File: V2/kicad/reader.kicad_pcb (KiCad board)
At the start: 2 copper layers, 42.5 x 62 mm, 93 parts, among them SW1 SW_Rezistance, SW2 SW_src, U1 STM32H523CET6, U2 MAX98357AETE+T, U3 MLD-TF PUSH-H18, U4 TCAN1057AVDRQ1, U5 ESD2CAN24-ES, U6 RJ-064-1, U7 MCP16301Hx-xCH, Y1 16MHz

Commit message: changed led red color resistor from 560 to 787
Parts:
- R15, R17: value 560 R -> 787 R
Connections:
- SW1 pad 2: (no net) -> unconnected-(SW1-Pad2)
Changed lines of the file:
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@@
 			)
 		)
-		(property "Value" "560 R"
+		(property "Value" "787 R"
 			(at 0 1.17 90)
 			(layer "F.Fab")
@@
 			)
 		)
-		(property "Datasheet" "https://jlc-prod-smt.oss-eu-central-1.aliyuncs.com/smtDataManualFile/8586178278474862592-C25126.pdf?response-content-disposition=attachment%3B%20filename%3DC25126.pdf%3B%20filename%2A%3DUTF-8%27%27C25126.pdf&x-oss-date=20260603T141942Z&x-oss-expires=1800&x-oss-security-token=CAISgAN1q6Ft5B2yfSjIr5rYAPaHqJFCjrvadU%2FFs1YWQtlZrr3lsTz2IHhMdHJsAOodtv0%2FmmhT6PkclqRLcbhpcmfjV%2BZHzLB8qeAa7RNB4J7b16cNrbH4M4H6aXeirtuwDsz9SNTCALjPD3nPii50x5bjaDymRCbLGJaViJlhHLN1Ow6jdmhpCctxLAlvo9NgFxm3D%2Fu2NQPwiWf9FVdhvhEG6Vly8qOi2MaRmFy8yFTx0b0SvJ%2BjYMrmPctoN9JnSdC5mfdzau3a1TJ84gRD0a5wkaVA1zbDs5bfISEIuUzebreLqY03dV4mOvdqIcMe8qigz88fk%2FfIioH6xyxKOexoSCnFTOiiupCcQLPyao9jLu6iayqViY7QaIOTqQohZmkAMwVOasAsI3Ngh4zF97Qt0cVNkXO9gWfLI8DtuMleWhqDHsNdntHD0eS19jklBdzSlusJRAJJUVBflCeKEaRNSAd3WGhEfM2%2BBt4QT30w5N2u00S8OSMIe8fo%2BKKWD5sagAFAjLTD0371Sd2gSdBnykA7MII9CzBs0TEnncOuMMFpZ7eWxtofkMZUw83MXKFT3yGfjS9fIlx%2Bre7vtwbXSVmucxBbZSJldeqhHVomhZC6FwsraIa5cFo%2FJ2rvy%2BYXQ1kdyLEoPt0fplni6hRiSJOL598AUZr9EPV4uuEaQBdebyAA&x-oss-signature-version=OSS4-HMAC-SHA256&x-oss-credential=STS.NYmKL3ENc9y1witWVCNVuAxNS%2F20260603%2Feu-central-1%2Foss%2Faliyun_v4_request&x-oss-signature=d1629a371fbf831c62f9f7f4032d37edb65e47d37709e76674d141769ad7b5bf"
+		(property "Datasheet" "https://www.lcsc.com/datasheet/C270582.pdf?spm=wm.sxq.inf.ggs___wm.fly.bg.0.xh&lcsc_vid=FVRbUlZVElUKAldUT1FbAVZWElcMUlFXR1FXBgVQElUxVlNeRlNeUVRXQFhZVTsOAxUeFF5JWBYZEEoKFBINSQcJGk4dAgUUFAk%3D"
 			(at 0 0 90)
 			(layer "F.Fab")
@@
 			)
 		)
-		(property "JLCPCB" "https://jlcpcb.com/partdetail/C25126"
+		(property "JLCPCB" "https://www.lcsc.com/product-detail/C270582.html"
 			(at 0 0 90)
 			(unlocked yes)
@@
 			)
 		)
-		(property "LCSC" "C25126"
+		(property "LCSC" "C270582"
 			(at 0 0 90)
 			(unlocked yes)
@@
 			(size 1.5 0.7)
 			(layers "F.Cu" "F.Mask" "F.Paste")
+			(net "unconnected-(SW1-Pad2)")
 			(pinfunction "2_2")
 			(pintype "passive+no_connect")
@@
 			)
 		)
-		(property "Value" "560 R"
+		(property "Value" "787 R"
 			(at 0 1.17 90)
 			(layer "F.Fab")
@@
 			)
 		)
-		(property "Datasheet" "https://jlc-prod-smt.oss-eu-central-1.aliyuncs.com/smtDataManualFile/8586178278474862592-C25126.pdf?response-content-disposition=attachment%3B%20filename%3DC25126.pdf%3B%20filename%2A%3DUTF-8%27%27C25126.pdf&x-oss-date=20260603T141942Z&x-oss-expires=1800&x-oss-security-token=CAISgAN1q6Ft5B2yfSjIr5rYAPaHqJFCjrvadU%2FFs1YWQtlZrr3lsTz2IHhMdHJsAOodtv0%2FmmhT6PkclqRLcbhpcmfjV%2BZHzLB8qeAa7RNB4J7b16cNrbH4M4H6aXeirtuwDsz9SNTCALjPD3nPii50x5bjaDymRCbLGJaViJlhHLN1Ow6jdmhpCctxLAlvo9NgFxm3D%2Fu2NQPwiWf9FVdhvhEG6Vly8qOi2MaRmFy8yFTx0b0SvJ%2BjYMrmPctoN9JnSdC5mfdzau3a1TJ84gRD0a5wkaVA1zbDs5bfISEIuUzebreLqY03dV4mOvdqIcMe8qigz88fk%2FfIioH6xyxKOexoSCnFTOiiupCcQLPyao9jLu6iayqViY7QaIOTqQohZmkAMwVOasAsI3Ngh4zF97Qt0cVNkXO9gWfLI8DtuMleWhqDHsNdntHD0eS19jklBdzSlusJRAJJUVBflCeKEaRNSAd3WGhEfM2%2BBt4QT30w5N2u00S8OSMIe8fo%2BKKWD5sagAFAjLTD0371Sd2gSdBnykA7MII9CzBs0TEnncOuMMFpZ7eWxtofkMZUw83MXKFT3yGfjS9fIlx%2Bre7vtwbXSVmucxBbZSJldeqhHVomhZC6FwsraIa5cFo%2FJ2rvy%2BYXQ1kdyLEoPt0fplni6hRiSJOL598AUZr9EPV4uuEaQBdebyAA&x-oss-signature-version=OSS4-HMAC-SHA256&x-oss-credential=STS.NYmKL3ENc9y1witWVCNVuAxNS%2F20260603%2Feu-central-1%2Foss%2Faliyun_v4_request&x-oss-signature=d1629a371fbf831c62f9f7f4032d37edb65e47d37709e76674d141769ad7b5bf"
+		(property "Datasheet" "https://www.lcsc.com/datasheet/C270582.pdf?spm=wm.sxq.inf.ggs___wm.fly.bg.0.xh&lcsc_vid=FVRbUlZVElUKAldUT1FbAVZWElcMUlFXR1FXBgVQElUxVlNeRlNeUVRXQFhZVTsOAxUeFF5JWBYZEEoKFBINSQcJGk4dAgUUFAk%3D"
 			(at 0 0 90)
 			(layer "F.Fab")
@@
 			)
 		)
-		(property "JLCPCB" "https://jlcpcb.com/partdetail/C25126"
+		(property "JLCPCB" "https://www.lcsc.com/product-detail/C270582.html"
 			(at 0 0 90)
 			(unlocked yes)
@@
 			)
 		)
-		(property "LCSC" "C25126"
+		(property "LCSC" "C270582"
 			(at 0 0 90)
 			(unlocked yes)
@@
 	)
 	(segment
+		(start 138.01 74.95)
+		(end 136.54 74.95)
+		(width 0.2)
+		(layer "F.Cu")
+		(net "/Net-(U1-VDDA)")
+	)
+	(segment
+		(start 138.65 75.59)
+		(end 138.01 74.95)
+		(width 0.2)
+		(layer "F.Cu")
+		(net "/Net-(U1-VDDA)")
+	)
+	(segment
+		(start 139.43595 73.28595)
+		(end 139.43595 75.00095)
+		(width 0.3)
+		(layer "F.Cu")
+		(net "/Net-(U1-VDDA)")
+	)
+	(segment
+		(start 139.7329 72.989)
+		(end 139.43595 73.28595)
+		(width 0.3)
+		(layer "F.Cu")
+		(net "/Net-(U1-VDDA)")
+	)
+	(segment
+		(start 140.8036 72.989)
+		(end 139.7329 72.989)
+		(width 0.3)
+		(layer "F.Cu")
+		(net "/Net-(U1-VDDA)")
+	)
+	(segment
+		(start 139.43595 75.00095)
+		(end 140.21 75.775)
+		(width 0.3)
+		(layer "F.Cu")
+		(net "/Net-(U1-VDDA)")
+	)
+	(segment
+		(start 138.65 75.59)
+		(end 138.8469 75.59)
+		(width 0.2)
+		(layer "F.Cu")
+		(net "/Net-(U1-VDDA)")
+	)
+	(segment
+		(start 138.8469 75.59)
+		(end 139.43595 75.00095)
+		(width 0.2)
+		(layer "F.Cu")
+		(net "/Net-(U1-VDDA)")
+	)
+	(segment
 		(start 164.51 35.63)
 		(end 164.51 35.314)
@@
 		(net "Net-(LED2-A2)")
 	)
-	(segment
-		(start 138.01 74.95)
-		(end 136.54 74.95)
-		(width 0.2)
-		(layer "F.Cu")
-		(net "/Net-(U1-VDDA)")
-	)
-	(segment
-		(start 138.65 75.59)
-		(end 138.01 74.95)
-		(width 0.2)
-		(layer "F.Cu")
-		(net "/Net-(U1-VDDA)")
-	)
-	(segment
-		(start 139.43595 73.28595)
-		(end 139.43595 75.00095)
-		(width 0.3)
-		(layer "F.Cu")
-		(net "/Net-(U1-VDDA)")
-	)
-	(segment
-		(start 139.7329 72.989)
-		(end 139.43595 73.28595)
-		(width 0.3)
-		(layer "F.Cu")
-		(net "/Net-(U1-VDDA)")
-	)
-	(segment
-		(start 140.8036 72.989)
-		(end 139.7329 72.989)
-		(width 0.3)
-		(layer "F.Cu")
-		(net "/Net-(U1-VDDA)")
-	)
-	(segment
-		(start 139.43595 75.00095)
-		(end 140.21 75.775)
-		(width 0.3)
-		(layer "F.Cu")
-		(net "/Net-(U1-VDDA)")
-	)
-	(segment
-		(start 138.65 75.59)
-		(end 138.8469 75.59)
-		(width 0.2)
-		(layer "F.Cu")
-		(net "/Net-(U1-VDDA)")
-	)
-	(segment
-		(start 138.8469 75.59)
-		(end 139.43595 75.00095)
-		(width 0.2)
-		(layer "F.Cu")
-		(net "/Net-(U1-VDDA)")
-	)
 	(zone

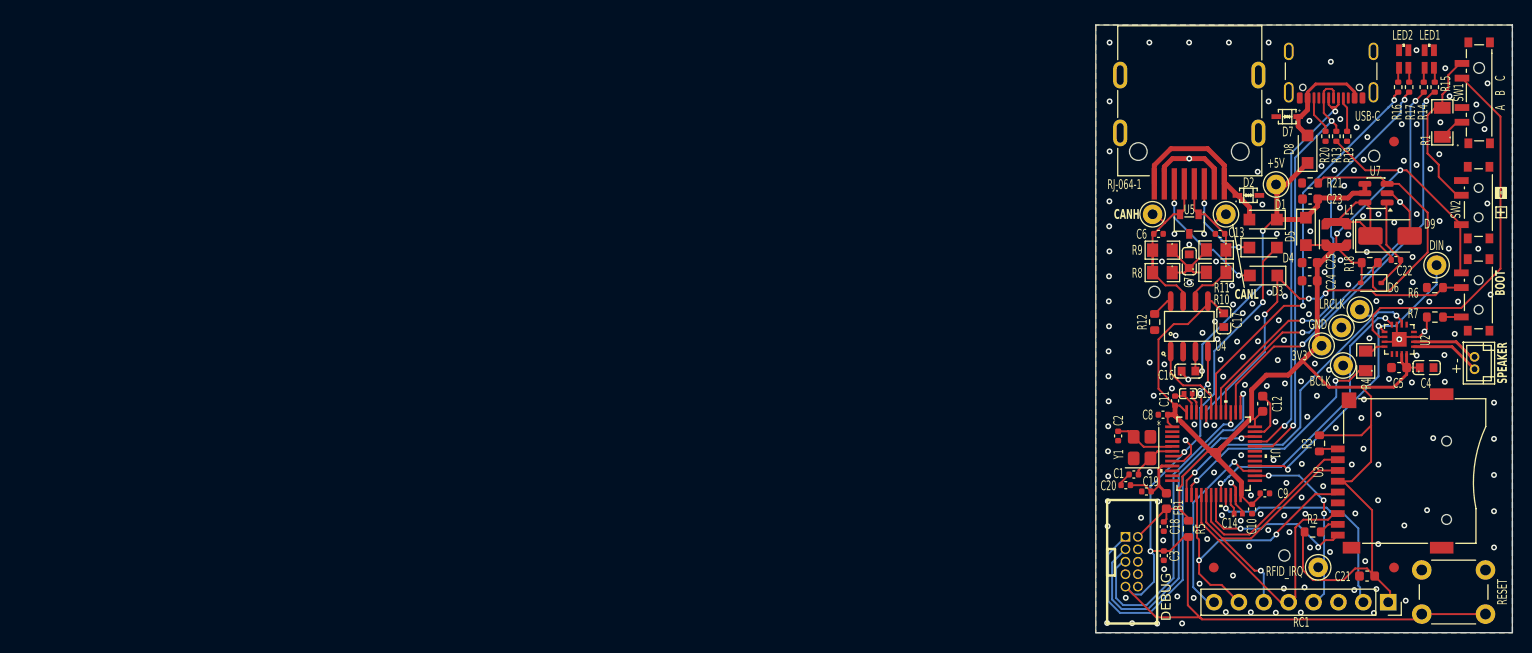
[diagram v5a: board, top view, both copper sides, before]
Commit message: changed size of pcb paper to A5 added labels and groups to schematic
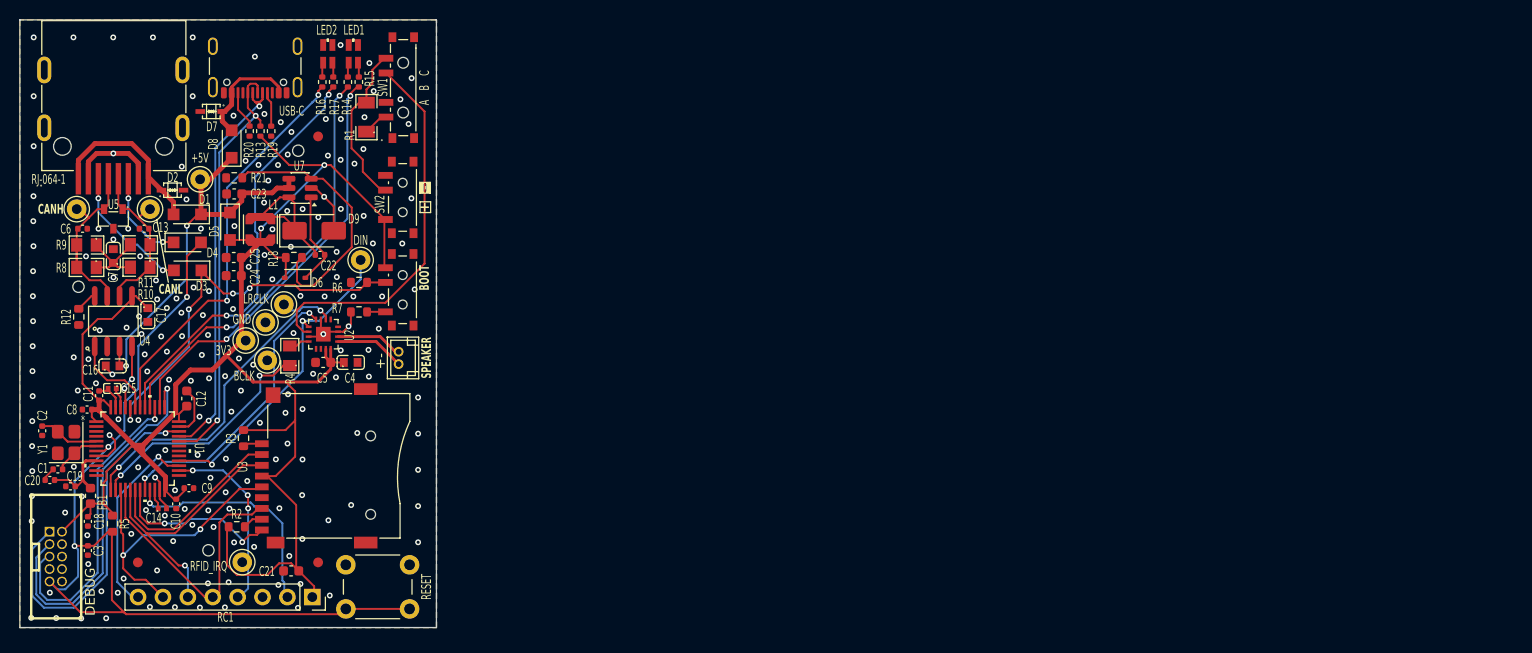
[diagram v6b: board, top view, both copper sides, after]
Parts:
- moved C11 109.8 mm to (31.3, 65.8)
- moved C12 109.8 mm to (40.3, 66.1)
- moved C13 109.8 mm to (35.9, 48.8)
- moved C16 109.8 mm to (32.7, 62.8)
- moved C17 109.8 mm to (36.3, 57.6)
- moved C20 109.8 mm to (26.3, 74.4)
- moved C21 109.8 mm to (50.9, 83.7)
- moved C22 109.8 mm to (53.8, 51.5)
- moved C23 109.8 mm to (45.1, 45.2)
- moved C6 109.8 mm to (29.6, 48.8)
- moved C8 109.8 mm to (30.1, 67.2)
- moved C9 109.8 mm to (40.5, 75.3)
- moved D3 109.8 mm to (40.4, 53.0)
- moved D7 109.8 mm to (42.8, 36.8)
- moved D8 109.8 mm to (44.8, 40.1)
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
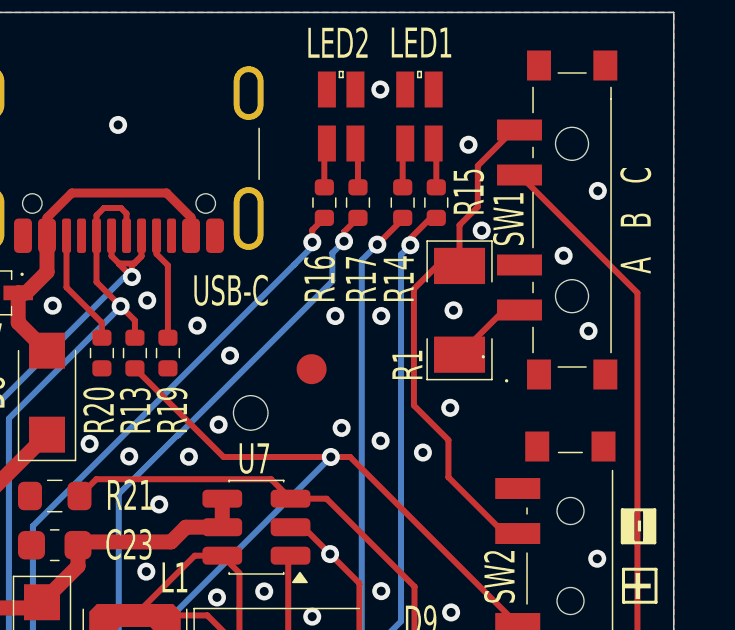
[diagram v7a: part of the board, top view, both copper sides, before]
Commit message: changed few components because of availability. moved thesis into this repository.
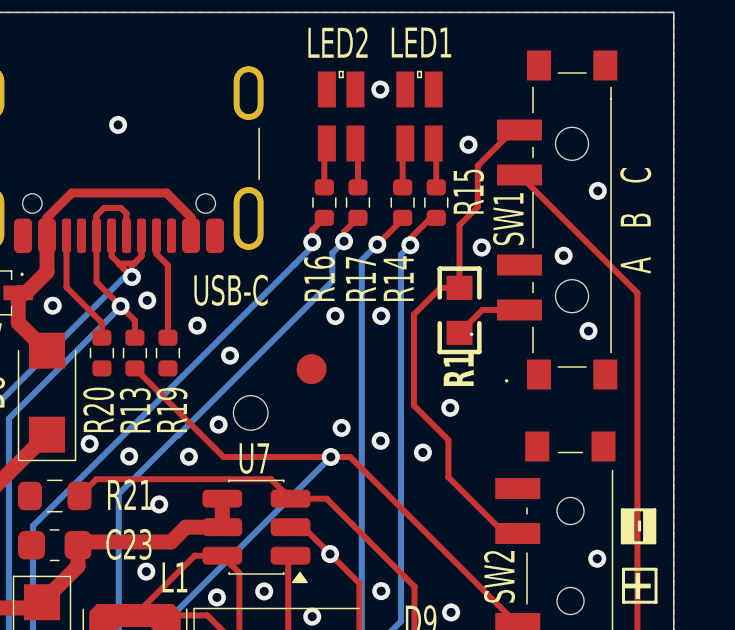
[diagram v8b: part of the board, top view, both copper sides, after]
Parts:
- C16, C17, C4: value CL10B104KC8NNNC -> CC0603KRX7R9BB104
- R1: value RC1206JR-07100KL -> 0603WAF1003T5E; footprint easyeda2kicad:R1206 -> easyeda2kicad:R0603
- R4: value RC0805FR-07634KL -> 0805W8F1501T5E
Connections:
- C17 pad 1: +3.3V -> GND
- C17 pad 2: GND -> +3.3V
- C4 pad 1: +3.3V -> GND
- C4 pad 2: GND -> +3.3V
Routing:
- net Net-(SW2-B): track 15.8 -> 16.4 mm
- net GND: vias 187 -> 186
